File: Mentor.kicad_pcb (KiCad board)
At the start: 2 copper layers, 50 x 90 mm, 41 parts, among them J1 CONN_01X02, J2 CONN_01X06, J3 CONN_01X09, J4 CONN_01X10, J5 CONN_01X02, J6 CONN_01X03, J7 CONN_01X09, Q1 PZT2222A, Q2 PZT2222A, Q3 STB55NF06T4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

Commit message: RTM, silmask to do
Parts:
- C4: moved to B.Cu
- C5: value C_Small -> 100n
- U1: footprint TO_SOT_Packages_SMD:SOT-223 -> TO_SOT_Packages_SMD:TO-263-3_TabPin4
- moved C3 20.9 mm to (189.0, 119.0), turned to 0 degrees
- moved C2 16.6 mm to (189.0, 123.0)
- moved C4 7.43 mm to (182.0, 118.0), turned to 270 degrees
- moved U1 4.00 mm to (174.0, 115.0)
- moved C1 0.50 mm to (168.0, 119.0)
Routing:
- net GND: track 210.6 -> 225.3 mm, vias 45 -> 47
- net +12V: track 112.7 -> 121.8 mm, vias 2 -> 1
- net +5V: track 120.1 -> 124.4 mm

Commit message: carte de control V1.0
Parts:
-  : renamed from TP1; value TEST -> (none)
-  : renamed from TP2; value TEST -> (none)
-  : renamed from TP3; value TEST -> (none)
-  : renamed from TP4; value TEST -> (none)
- J1, J5: value CONN_01X02 -> (none)
- J2: value CONN_01X06 -> (none)
- J3, J7: value CONN_01X09 -> (none)
- J4: value CONN_01X10 -> (none)
- J6: value CONN_01X03 -> (none)
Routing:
- net GND: track 225.3 -> 292.4 mm, vias 47 -> 61
- net +12V: track 121.8 -> 117.1 mm
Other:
- board text added: "+12V in Gnd"
- board text added: "50V Gnd"
- board text added: "From Alexandrie Control Brd"
- board text added: "From Amp"
- board text added: "Gnd +12V Fan"
- board text added: "Gnd C°-> Gnd U -> I -> Gnd Gnd PTT/Bias Disable Gnd +12V"
- board text added: "Led_K Led_A Vee E2 Vdd Vss VO RS RW E1 DB0 DB1 DB2 DB3 DB4 DB5 DB6 DB7"
- board text added: "REFL FWD Gnd +12V TXRX_Rly TX/RX Status"

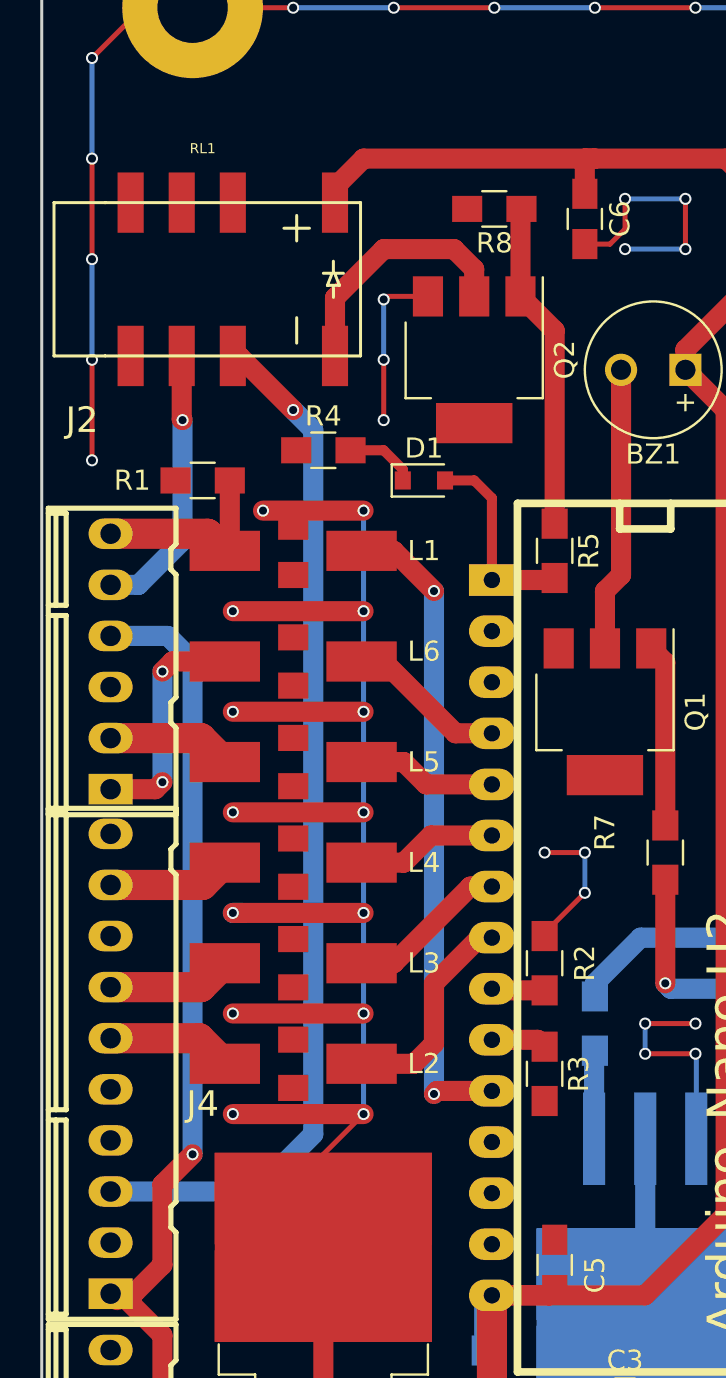
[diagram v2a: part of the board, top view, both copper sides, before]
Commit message: add a THT relay, cleaning silk, shielding mask zone added
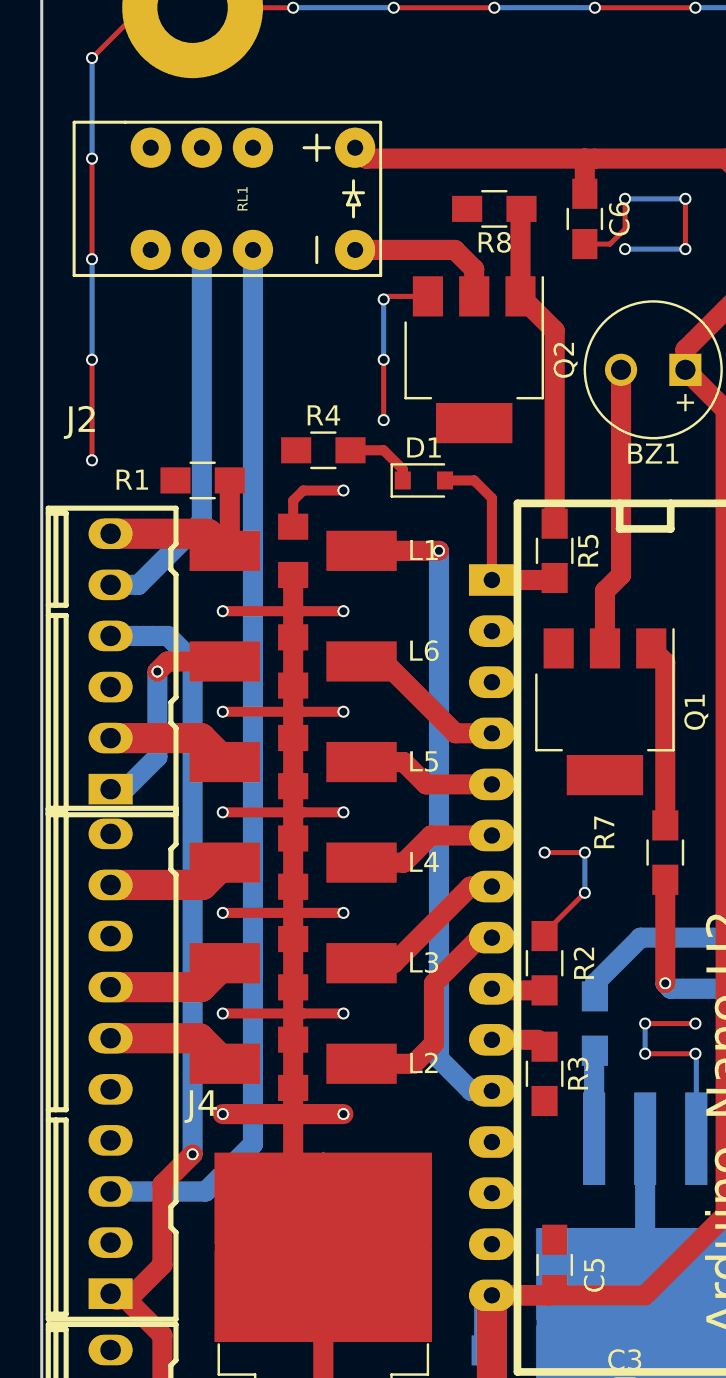
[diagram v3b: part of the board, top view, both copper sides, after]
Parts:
- J1, J5: value (none) -> CONN_01X02
- J2: value (none) -> CONN_01X06
- J3, J7: value (none) -> CONN_01X09
- J4: value (none) -> CONN_01X10
- J6: value (none) -> CONN_01X03
- RL1: footprint 2_Form_C_Relay:smd_2_formC -> 2_Form_C_Relay:THT_2_formC
- TP1, TP2, TP3, TP4: renamed from  ; value (none) -> TEST
- moved RL1 4.12 mm to (170.5, 59.5)
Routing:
- net Net-(J2-Pad5): track 13.7 -> 19.3 mm, vias 1 -> 0
- net Net-(Q2-Pad2): track 12.6 -> 7.67 mm
- net +5V: track 124.4 -> 121.8 mm
- net GND: track 292.4 -> 291.6 mm, vias 61 -> 60
- net Net-(J2-Pad1): track 11.5 -> 10.8 mm, vias 2 -> 1
- net Net-(J4-Pad3): track 51.8 -> 52.5 mm, vias 1 -> 0
- net Net-(L1-Pad3): vias 2 -> 1
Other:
- board text added: "Gnd C°-> Gnd U -> I -> Gnd PTT/ Gnd Bias Disable Gnd +12V"
- board text removed: "Gnd C°-> Gnd U -> I -> Gnd Gnd PTT/Bias Disable Gnd +12V"

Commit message: RTM 1
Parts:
- RL1: value EC2-5NU -> EE2-12NU
- moved TP1 10.3 mm to (165.0, 40.0)
- moved TP2 10.3 mm to (205.0, 40.0)
- moved C6 9.00 mm to (178.2, 58.6)
- moved C2 3.91 mm to (186.0, 120.5), turned to 90 degrees
- moved TP3 3.54 mm to (165.0, 130.0)
- moved TP4 3.54 mm to (205.0, 130.0)
- moved C3 2.55 mm to (189.5, 121.5), turned to 90 degrees
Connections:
- C6 pad 1: +5V -> +12V
- RL1 pad 1: +5V -> +12V
- RL1 pad 3: (no net) -> Net-(J4-Pad3)
- RL1 pad 4: (no net) -> Net-(J2-Pad5)
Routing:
- net +5V: track 121.8 -> 93.5 mm
- net +12V: track 117.1 -> 136.3 mm, vias 1 -> 2
- net GND: track 291.6 -> 302.9 mm, vias 60 -> 68
- net Net-(J4-Pad3): track 52.5 -> 57.6 mm
- net Net-(J2-Pad5): track 19.3 -> 24.1 mm
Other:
- board size 50 x 90 mm -> 50 x 100 mm

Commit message: Readme cleaning, add 2 3D pictures
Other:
- board text added: "FWD REFL Gnd +12V TXRX_Rly TX/RX Status"
- board text added: "Gnd +12V in"
- board text removed: "+12V in Gnd"
- board text removed: "REFL FWD Gnd +12V TXRX_Rly TX/RX Status"
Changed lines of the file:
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@@
   )
   (setup
-    (last_trace_width 1)
+    (last_trace_width 0.25)
     (user_trace_width 0.5)
     (user_trace_width 1)
@@
     (pad 2 thru_hole oval (at 1.27 -0.0762 90) (size 1.524 2.1971) (drill 1.016) (layers *.Cu *.Mask F.SilkS)
       (net 4 GND))
-    (model walter/conn_kk100/22-23-2021.wrl
-      (at (xyz 0 0 0))
-      (scale (xyz 1 1 1))
-      (rotate (xyz 0 0 0))
-    )
     (model ../../../../../../Users/Marco/Documents/Kicad/Projets/Mentor/Modules/conn_kk100.pretty/packages3d/kk100_22-23-2021.wrl
       (at (xyz 0 0 0))
       (scale (xyz 1 1 1))
-      (rotate (xyz 0 0 0))
+      (rotate (xyz 0 0 180))
     )
   )
@@
       (at (xyz 0 0 0))
       (scale (xyz 1 1 1))
-      (rotate (xyz 0 0 0))
+      (rotate (xyz 0 0 180))
     )
   )
@@
     (pad 2 thru_hole oval (at -3.81 -0.0762 90) (size 1.524 2.1971) (drill 1.016) (layers *.Cu *.Mask F.SilkS)
       (net 10 "Net-(J2-Pad2)"))
-    (model walter/conn_kk100/22-23-2061.wrl
-      (at (xyz 0 0 0))
-      (scale (xyz 1 1 1))
-      (rotate (xyz 0 0 0))
-    )
     (model ../../../../../../Users/Marco/Documents/Kicad/Projets/Mentor/Modules/conn_kk100.pretty/packages3d/kk100_22-23-2061.wrl
       (at (xyz 0 0 0))
       (scale (xyz 1 1 1))
-      (rotate (xyz 0 0 0))
+      (rotate (xyz 0 0 180))
     )
   )
@@
     (pad 2 thru_hole oval (at -8.89 -0.0762 90) (size 1.524 2.1971) (drill 1.016) (layers *.Cu *.Mask F.SilkS)
       (net 4 GND))
-    (model walter/conn_kk100/22-23-2101.wrl
-      (at (xyz 0 0 0))
-      (scale (xyz 1 1 1))
-      (rotate (xyz 0 0 0))
-    )
     (model ../../../../../../Users/Marco/Documents/Kicad/Projets/Mentor/Modules/conn_kk100.pretty/packages3d/kk100_22-23-2101.wrl
       (at (xyz 0 0 0))
       (scale (xyz 1 1 1))
-      (rotate (xyz 0 0 0))
+      (rotate (xyz 0 0 180))
     )
   )
@@
     (pad 2 thru_hole oval (at 1.27 -0.0762 270) (size 1.524 2.1971) (drill 1.016) (layers *.Cu *.Mask F.SilkS)
       (net 4 GND))
-    (model walter/conn_kk100/22-23-2021.wrl
-      (at (xyz 0 0 0))
-      (scale (xyz 1 1 1))
-      (rotate (xyz 0 0 0))
-    )
     (model ../../../../../../Users/Marco/Documents/Kicad/Projets/Mentor/Modules/conn_kk100.pretty/packages3d/kk100_22-23-2021.wrl
       (at (xyz 0 0 0))
       (scale (xyz 1 1 1))
-      (rotate (xyz 0 0 0))
+      (rotate (xyz 0 0 180))
     )
   )
@@
     (pad 2 thru_hole oval (at 0 -0.0762 270) (size 1.524 2.1971) (drill 1.016) (layers *.Cu *.Mask F.SilkS)
       (net 3 +12V))
-    (model walter/conn_kk100/22-23-2031.wrl
-      (at (xyz 0 0 0))
-      (scale (xyz 1 1 1))
-      (rotate (xyz 0 0 0))
-    )
     (model ../../../../../../Users/Marco/Documents/Kicad/Projets/Mentor/Modules/conn_kk100.pretty/packages3d/kk100_22-23-2031.wrl
       (at (xyz 0 0 0))
       (scale (xyz 1 1 1))
-      (rotate (xyz 0 0 0))
+      (rotate (xyz 0 0 180))
     )
   )
@@
       (net 25 LCDE1))
     (pad 2 thru_hole oval (at -7.62 -0.0762 270) (size 1.524 2.1971) (drill 1.016) (layers *.Cu *.Mask F.SilkS))
-    (model walter/conn_kk100/22-23-2091.wrl
-      (at (xyz 0 0 0))
-      (scale (xyz 1 1 1))
-      (rotate (xyz 0 0 0))
-    )
     (model ../../../../../../Users/Marco/Documents/Kicad/Projets/Mentor/Modules/conn_kk100.pretty/packages3d/kk100_22-23-2091.wrl
       (at (xyz 0 0 0))
       (scale (xyz 1 1 1))
-      (rotate (xyz 0 0 0))
+      (rotate (xyz 0 0 180))
     )
   )
@@
     (model ${KISYS3DMOD}/TO_SOT_Packages_SMD.3dshapes/SOT-223.wrl
       (at (xyz 0 0 0))
-      (scale (xyz 0.4 0.4 0.4))
-      (rotate (xyz 0 0 90))
+      (scale (xyz 1 1 1))
+      (rotate (xyz 0 0 0))
     )
   )
@@
     (effects (font (size 1 1) (thickness 0.25)) (justify mirror))
   )
-  (gr_text "REFL\nFWD\nGnd\n+12V\nTXRX_Rly\nTX/RX Status" (at 165.5 82.5) (layer B.SilkS)
+  (gr_text "FWD\nREFL\nGnd\n+12V\nTXRX_Rly\nTX/RX Status" (at 165.5 82.5) (layer B.SilkS)
     (effects (font (size 1.5 1.5) (thickness 0.3)) (justify right mirror))
   )
@@
     (effects (font (size 1.5 1.5) (thickness 0.3)) (justify right mirror))
   )
-  (gr_text "+12V in\nGnd     " (at 175 118) (layer B.SilkS)
-    (effects (font (size 1.5 1.5) (thickness 0.3)) (justify left mirror))
+  (gr_text "Gnd\n+12V in    " (at 166 118) (layer B.SilkS)
+    (effects (font (size 1.5 1.5) (thickness 0.3)) (justify right mirror))
   )
   (gr_line (start 160 135) (end 210 135) (angle 90) (layer Edge.Cuts) (width 0.15))
@@
   (segment (start 170.15 76.95) (end 170.1 77) (width 0.5) (layer F.Cu) (net 7))
   (segment (start 170 76.9) (end 170.1 77) (width 0.5) (layer F.Cu) (net 7))
-  (segment (start 167.96 56.96) (end 167.96 62.04) (width 1) (layer B.Cu) (net 8) (status C00000))
+  (segment (start 167.96 56.96) (end 167.96 62.04) (width 1) (layer B.Cu) (net 8))
   (segment (start 167.96 62.04) (end 167.96 65.04) (width 1) (layer B.Cu) (net 8))
   (segment (start 166 77) (end 164.31 78.69) (width 1) (layer B.Cu) (net 8))
@@
   (segment (start 163.4238 98.69) (end 167.91 98.69) (width 1.5) (layer F.Cu) (net 16))
   (segment (start 167.91 98.69) (end 169.1 97.5) (width 1.5) (layer F.Cu) (net 16))
-  (segment (start 170.5 56.96) (end 170.5 62.04) (width 1) (layer B.Cu) (net 17) (status C00000))
+  (segment (start 170.5 56.96) (end 170.5 62.04) (width 1) (layer B.Cu) (net 17))
   (segment (start 170.5 62.04) (end 170.5 106.5) (width 1) (layer B.Cu) (net 17))
   (segment (start 168.15 108.85) (end 163.4238 108.85) (width 1) (layer B.Cu) (net 17))

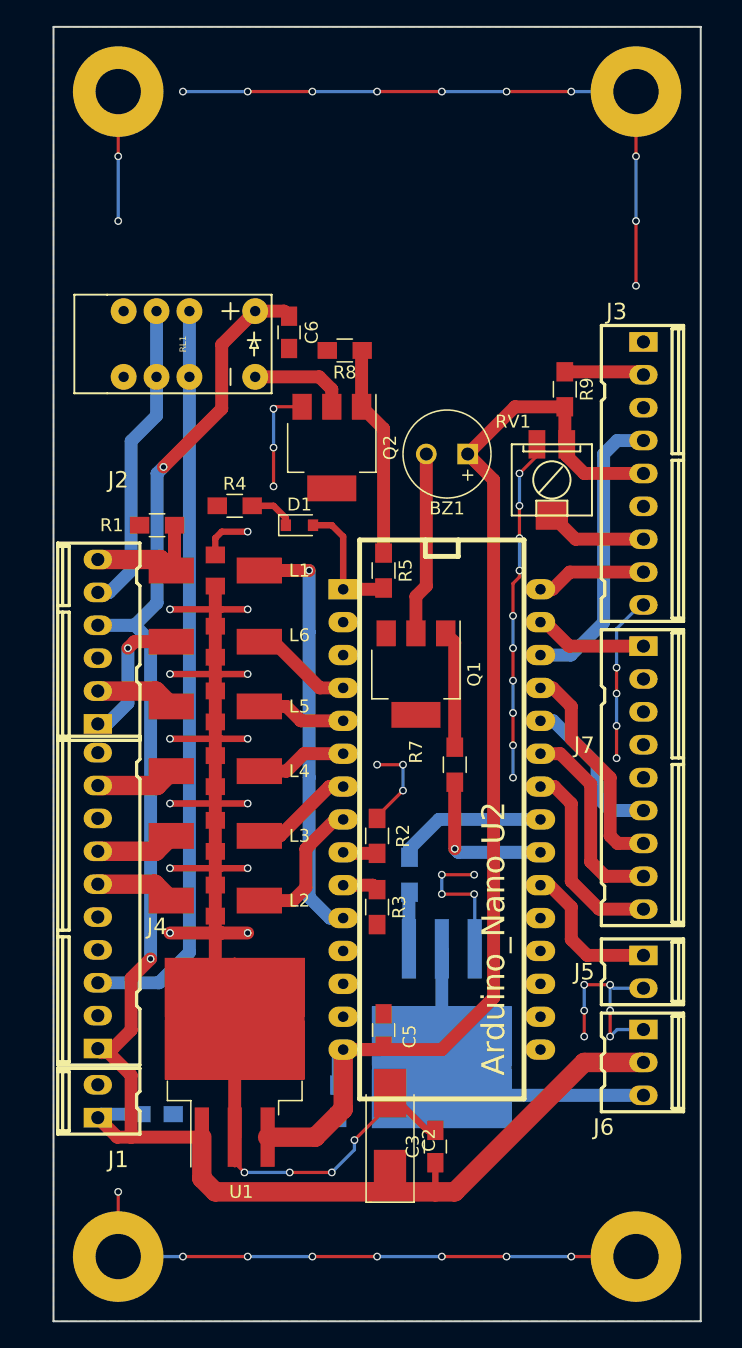
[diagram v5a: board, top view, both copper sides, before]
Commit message: new ferrite footprint, minor routing changes
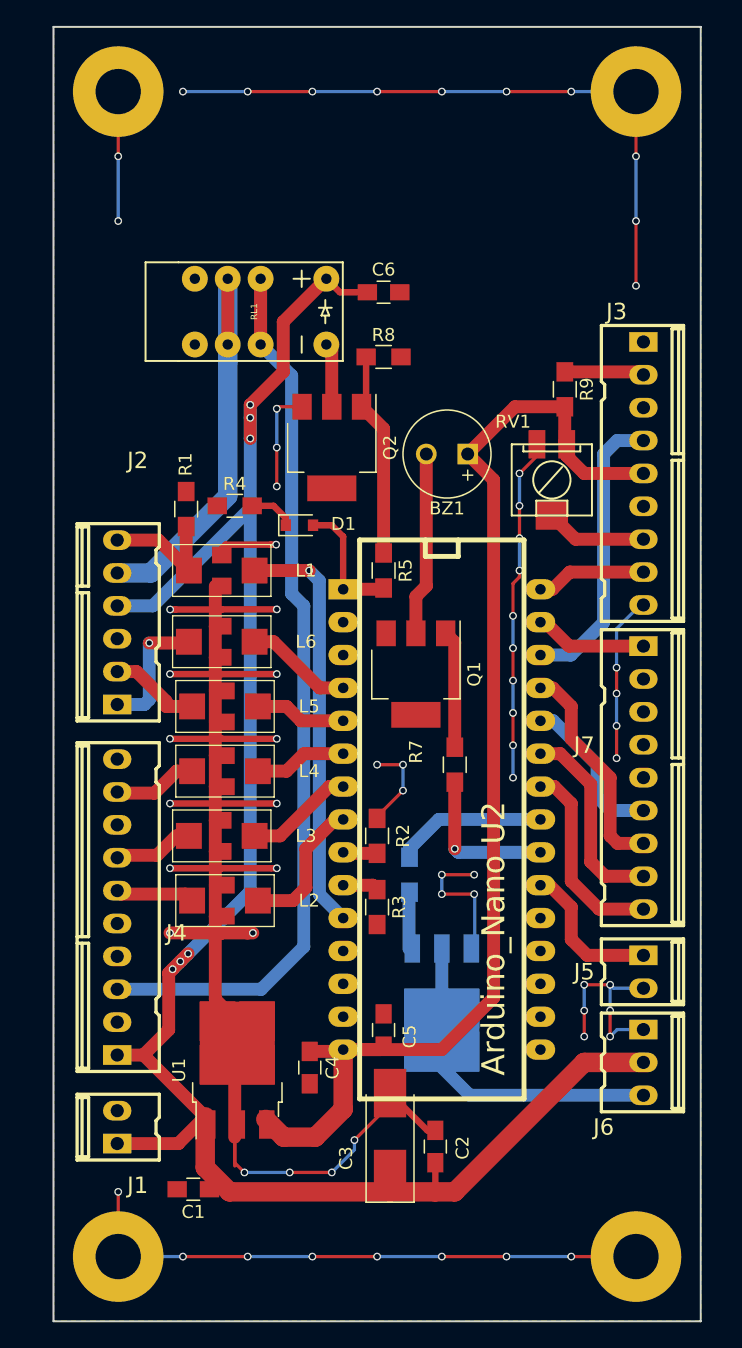
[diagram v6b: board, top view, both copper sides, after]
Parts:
- C1, C4: moved to F.Cu
- Q3: value STB55NF06T4 -> IRFR3303; footprint TO_SOT_Packages_SMD:TO-263-3_TabPin4 -> TO_SOT_Packages_SMD:TO-252-3_TabPin2
- RL1: value EE2-12NU -> EC2-12NU
- U1: value LD29150DT50R -> KA78M05_TO252; footprint TO_SOT_Packages_SMD:TO-263-3_TabPin4 -> TO_SOT_Packages_SMD:TO-252-3_TabPin2
- moved C6 7.93 mm to (185.5, 55.5), turned to 0 degrees
- moved C1 6.44 mm to (170.8, 124.8), turned to 180 degrees
- moved RL1 6.04 mm to (176.0, 57.0)
- moved C4 3.41 mm to (179.8, 115.4)
- moved R8 3.04 mm to (185.5, 60.5), turned to 0 degrees
- moved R1 2.57 mm to (170.2, 72.2), turned to 90 degrees
- moved J1 2.50 mm to (165.0, 120.0)
- moved J2 2.12 mm to (165.0, 81.0)
- moved Q3 1.60 mm to (190.0, 110.4)
- moved J4 1.58 mm to (165.0, 103.0)
- moved L2 0.75 mm to (173.2, 102.5)
- moved L4 0.75 mm to (173.2, 92.5)
- moved L5 0.75 mm to (173.2, 87.5)
- moved U1 0.63 mm to (174.2, 115.6)
- moved L1 0.50 mm to (173.0, 77.0)
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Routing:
- net +12V: track 136.3 -> 156.1 mm, vias 2 -> 6
- net Net-(J4-Pad3): track 57.6 -> 73.8 mm
- net Net-(J2-Pad5): track 24.1 -> 33.4 mm
- net GND: track 302.9 -> 308.6 mm
- net Net-(Q2-Pad2): track 7.67 -> 4.98 mm
- net Net-(J2-Pad2): track 6.17 -> 7.13 mm
- net Net-(J2-Pad1): track 10.8 -> 10.1 mm
- net Net-(L1-Pad3): track 32.4 -> 31.8 mm
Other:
- board text added: "TX/RX Status TXRX_Rly +12V Gnd REFL FWD"
- board text removed: "FWD REFL Gnd +12V TXRX_Rly TX/RX Status"
